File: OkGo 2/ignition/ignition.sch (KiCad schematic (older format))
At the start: 30 parts

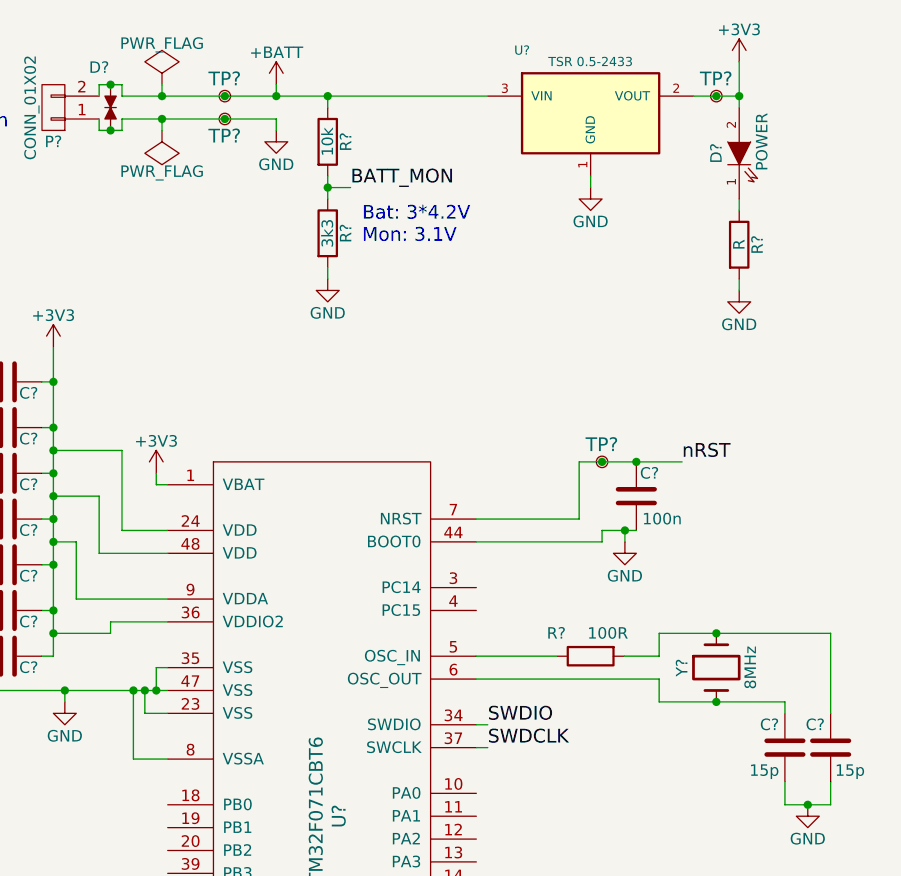
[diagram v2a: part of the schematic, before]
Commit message: Moved xtal drive resistors. Fixes #15
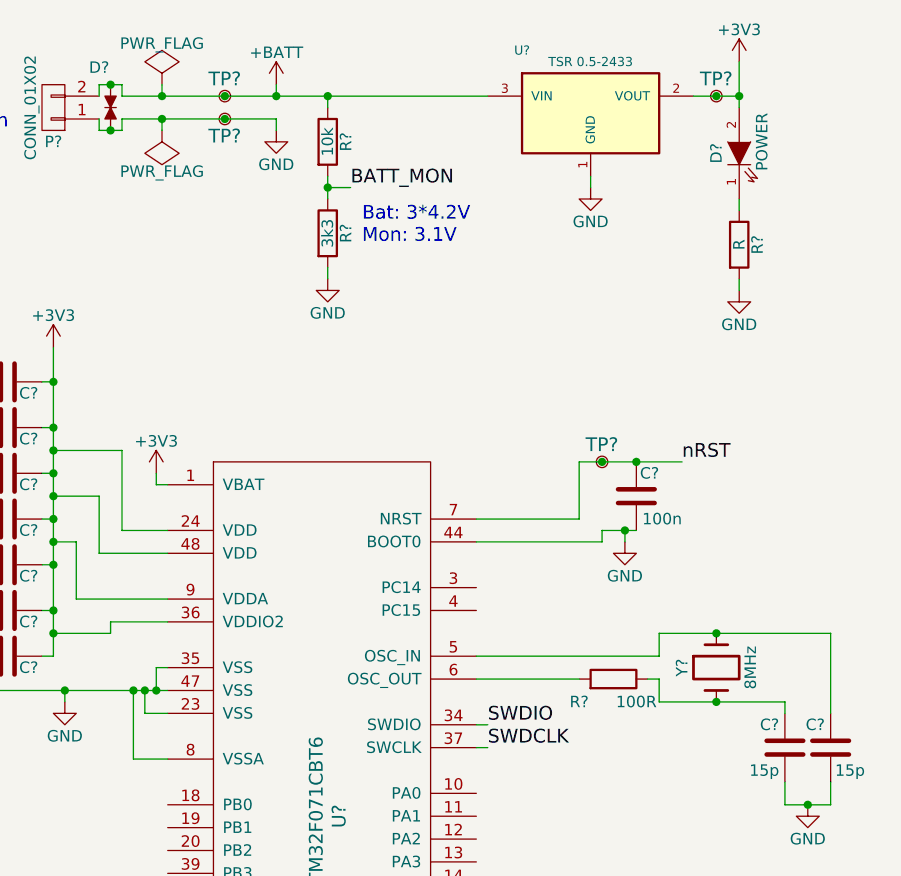
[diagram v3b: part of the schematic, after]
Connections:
- net at C?.1, Y?.1: now also U?.5 (OSC_IN); no longer R?.2
- net at C?.1, Y?.2: now also R?.1; no longer U?.6 (OSC_OUT)
- new net: R?.2, U?.6 (OSC_OUT)
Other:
- moved on the sheet: R?
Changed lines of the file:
@@
 L R R?
 U 1 1 55630D1D
-P 3450 3400
-F 0 "R?" V 3350 3550 50  0000 C CNN
-F 1 "100R" V 3350 3325 50  0000 C CNN
-F 2 "Resistors_SMD:R_0805_HandSoldering" V 3380 3400 30  0001 C CNN
-F 3 "" H 3450 3400 30  0000 C CNN
-F 4 "2331783" H 3450 3400 60  0001 C CNN "Farnell"
-	1    3450 3400
-	0    -1   1    0
+P 3550 3500
+F 0 "R?" V 3450 3350 50  0000 C CNN
+F 1 "100R" V 3450 3600 50  0000 C CNN
+F 2 "Resistors_SMD:R_0805_HandSoldering" V 3480 3500 30  0001 C CNN
+F 3 "" H 3550 3500 30  0000 C CNN
+F 4 "2331783" H 3550 3500 60  0001 C CNN "Farnell"
+	1    3550 3500
+	0    1    -1   0
 $EndComp
 $Comp
@@
 	1400 1050 1575 1050
 Wire Wire Line
-	1575 1050 2075 1050
+	1575 1050 1850 1050
+Wire Wire Line
+	1850 1050 2075 1050
 Wire Wire Line
 	2075 950  2075 900
@@
 Connection ~ 3600 2850
 Wire Wire Line
-	3400 2550 3650 2550
+	3400 2550 3500 2550
+Wire Wire Line
+	3500 2550 3650 2550
 Wire Wire Line
 	3650 2550 3850 2550
@@
 	3500 2900 2950 2900
 Wire Wire Line
-	2950 3400 3300 3400
-Wire Wire Line
-	3600 3400 3750 3400
+	2950 3400 3750 3400
 Wire Wire Line
 	3750 3400 3750 3300
@@
 Wire Wire Line
 	3750 3600 3750 3500
-Wire Wire Line
-	3750 3500 2950 3500
 Wire Wire Line
 	4300 3600 4300 3650
@@
 	1150 3550 1150 3600
 Wire Wire Line
-	3900 950  4100 950
+	3900 950  4000 950
+Wire Wire Line
+	4000 950  4100 950
 Wire Wire Line
 	1550 2600 1550 2650
@@
 	1400 950  1575 950
 Wire Wire Line
-	1575 950  2075 950
+	1575 950  1850 950
+Wire Wire Line
+	1850 950  2075 950
 Wire Wire Line
 	2075 950  2300 950
@@
 $EndComp
 Connection ~ 3500 2550
+Wire Wire Line
+	2950 3500 3400 3500
+Wire Wire Line
+	3750 3500 3700 3500
 $EndSCHEMATC

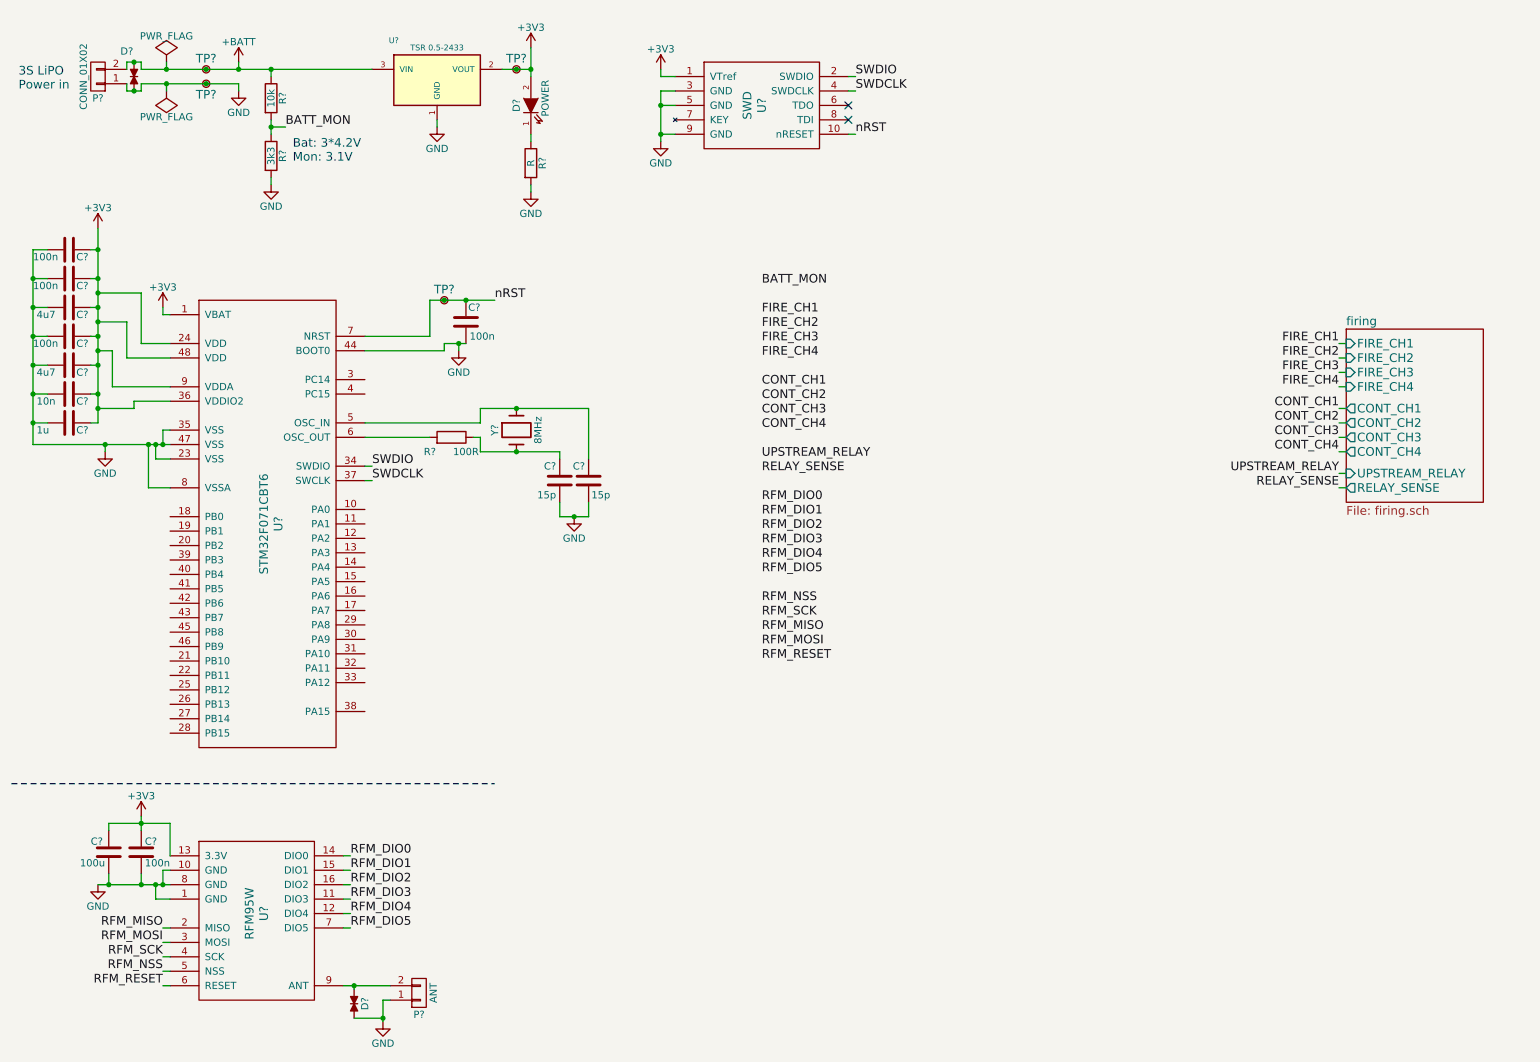
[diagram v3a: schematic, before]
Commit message: Specced/valued/footprinted a lot of parts
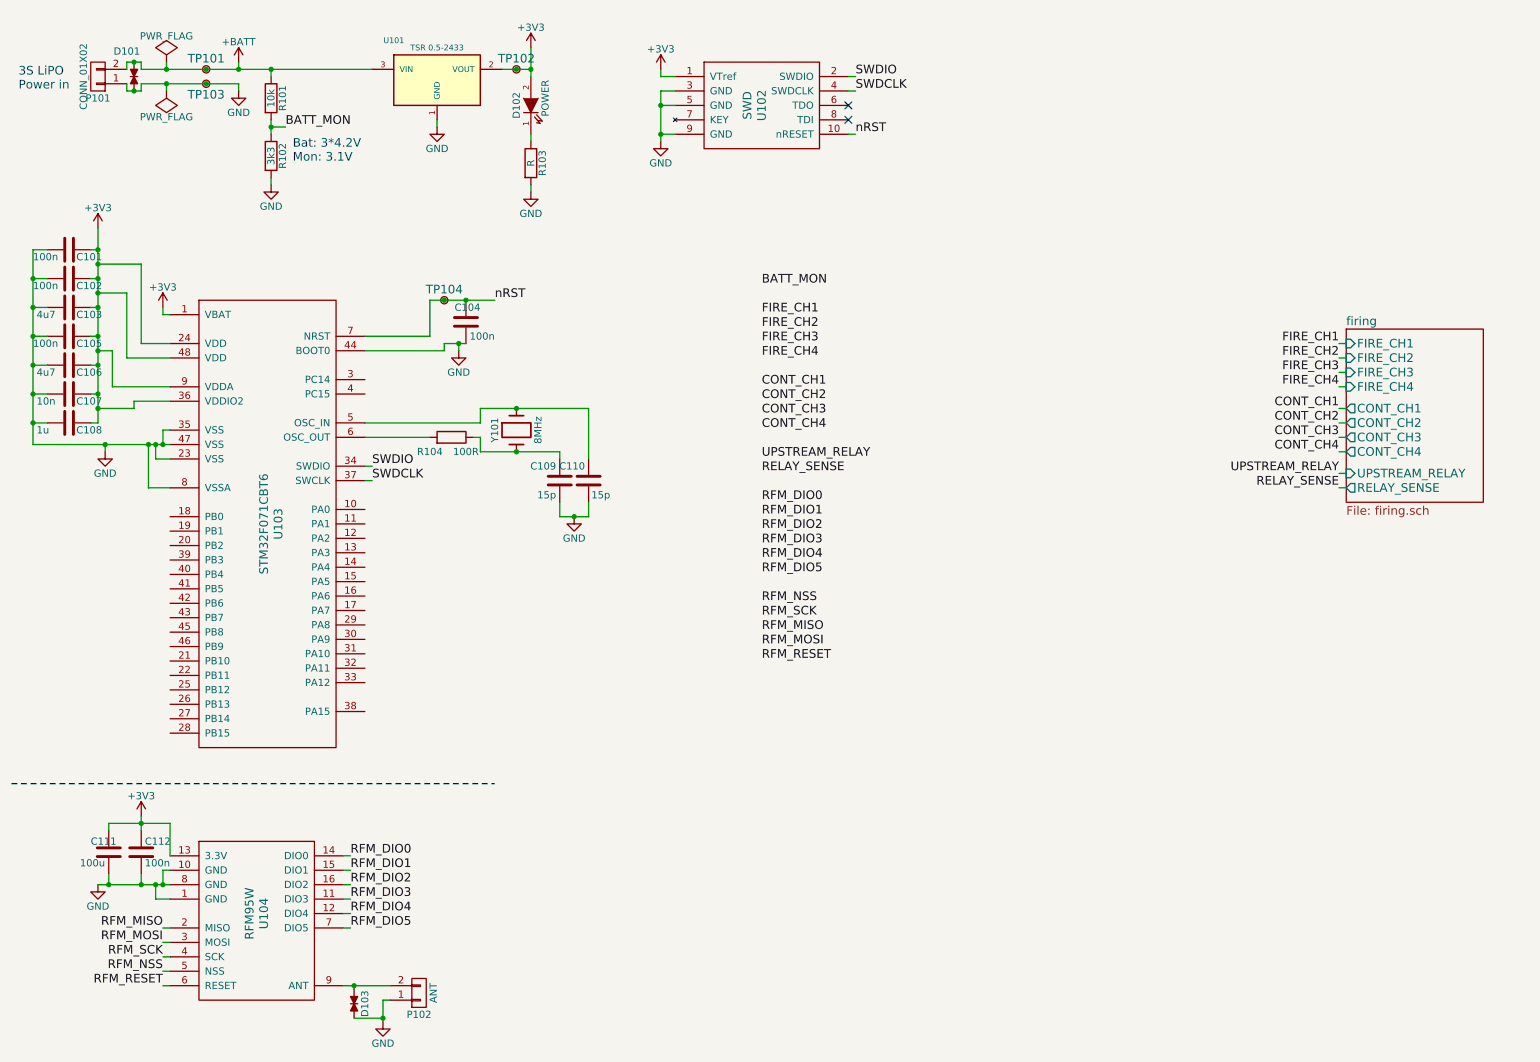
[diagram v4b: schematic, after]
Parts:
- R101: renamed from R?; Farnell 2331808 -> 9237755
- R102: renamed from R?; Farnell 2331802 -> 9237682
- U102: renamed from U?; footprint (none) -> common:FTSH-105-01-F-D-K
- U103: renamed from U?; footprint (none) -> Housings_QFP:LQFP-48_7x7mm_Pitch0.5mm; Farnell (none) -> 2432093
- gave numbers to parts that had none: 26

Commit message: Lots and lots of part selections and small mods
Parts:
- removed P102: ANT, symbol CONN_01X02
- added BT?: LiPO_3S, symbol LiPO_3S
- added F?: FUSE, symbol FUSE
- added P?: SMA, common:SMA-142-0701-801, symbol SMA
- added P? (x2): CHARGE_CASE, symbol CONN_01X04
- added P?: BATT, symbol CONN_01X02
- added P?: CHARGE_JST_XH, symbol CONN_01X04
- added SW?: Latching Push, symbol SPST_small
- P101: value CONN_01X02 -> BATT
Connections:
- net +BATT: now also F?.2; no longer D101.1, P101.2 (P2)
- net GND: now also P?.2 (GND), P?.3 (GND), P?.4 (GND), P?.5 (GND)
- net at D103.1, U104.9 (ANT): now also P?.1 (RF)
- new net: D101.1, F?.1, P101.2 (P2)
- new net: BT?.1, P?.1 (P1), P?.1 (P1)
- new net: BT?.2, P?.2 (P2)
- new net: BT?.3, P?.3 (P3)
- new net: BT?.4, P?.4 (P4), SW?.1
- new net: P?.2 (P2), SW?.2
- new net: P?.1 (P1), P?.1 (P1)
- new net: P?.2 (P2), P?.2 (P2)
- new net: P?.3 (P3), P?.3 (P3)
- new net: P?.4 (P4), P?.4 (P4)
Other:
- note removed: "3S LiPO\nPower in"
- moved on the sheet: C101, C102, C103, C104, C105, C106, C107, C108, C109, C110, C111, C112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

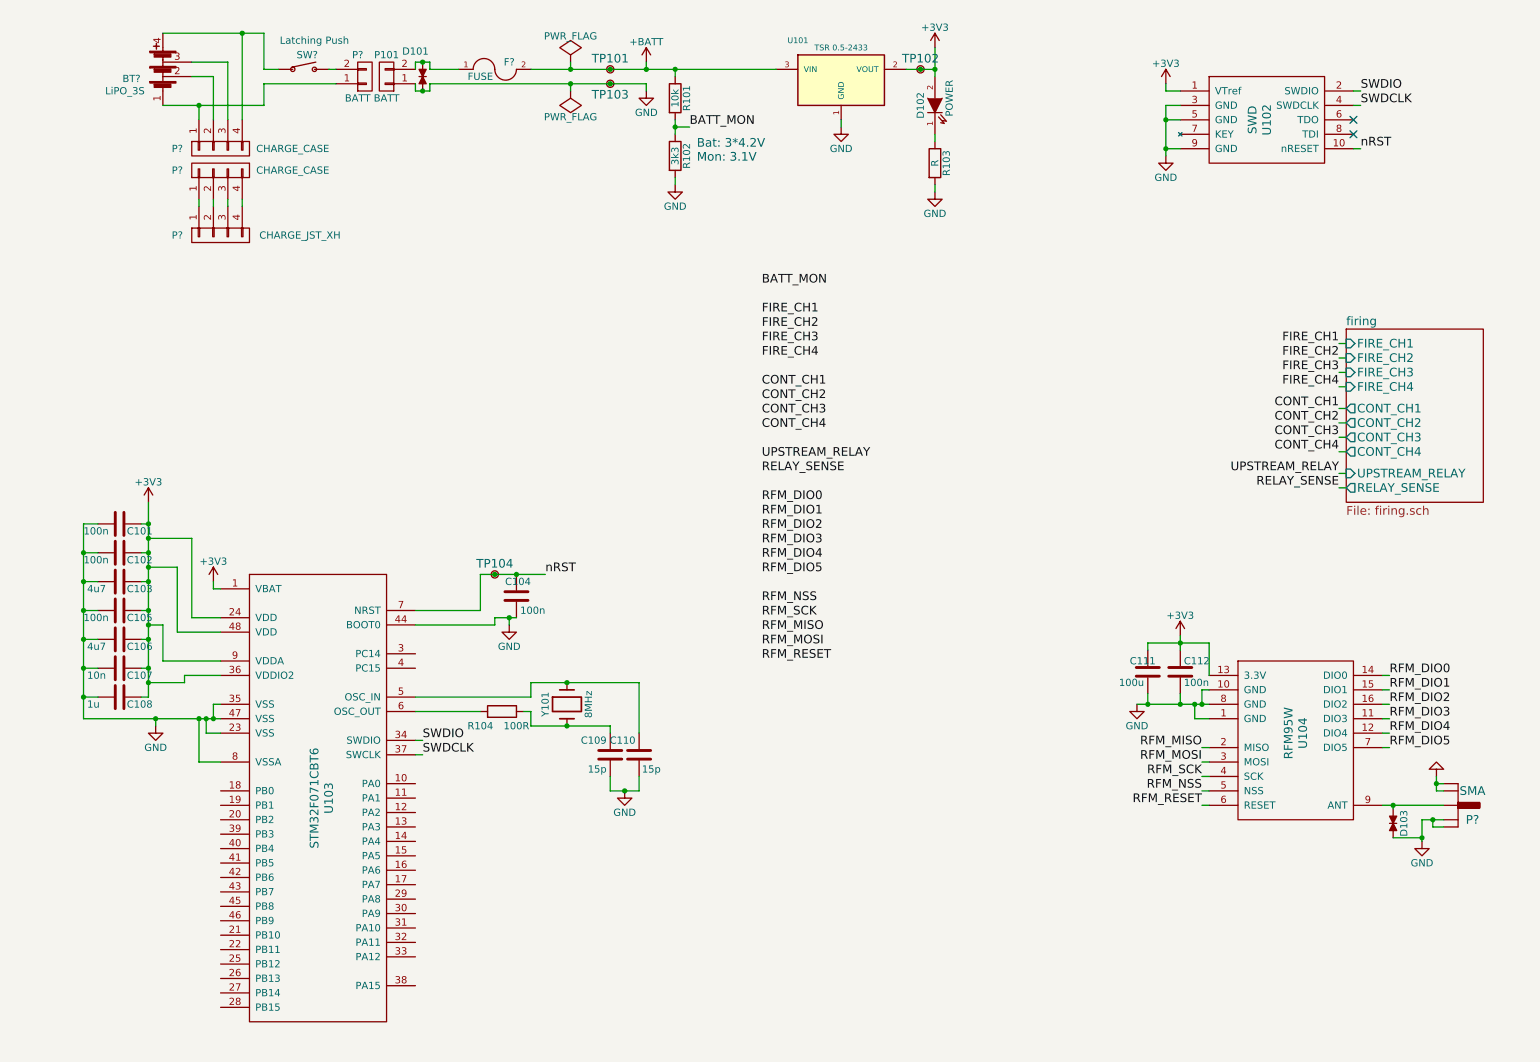
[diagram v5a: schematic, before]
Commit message: New power buttons and arm/disarm LED
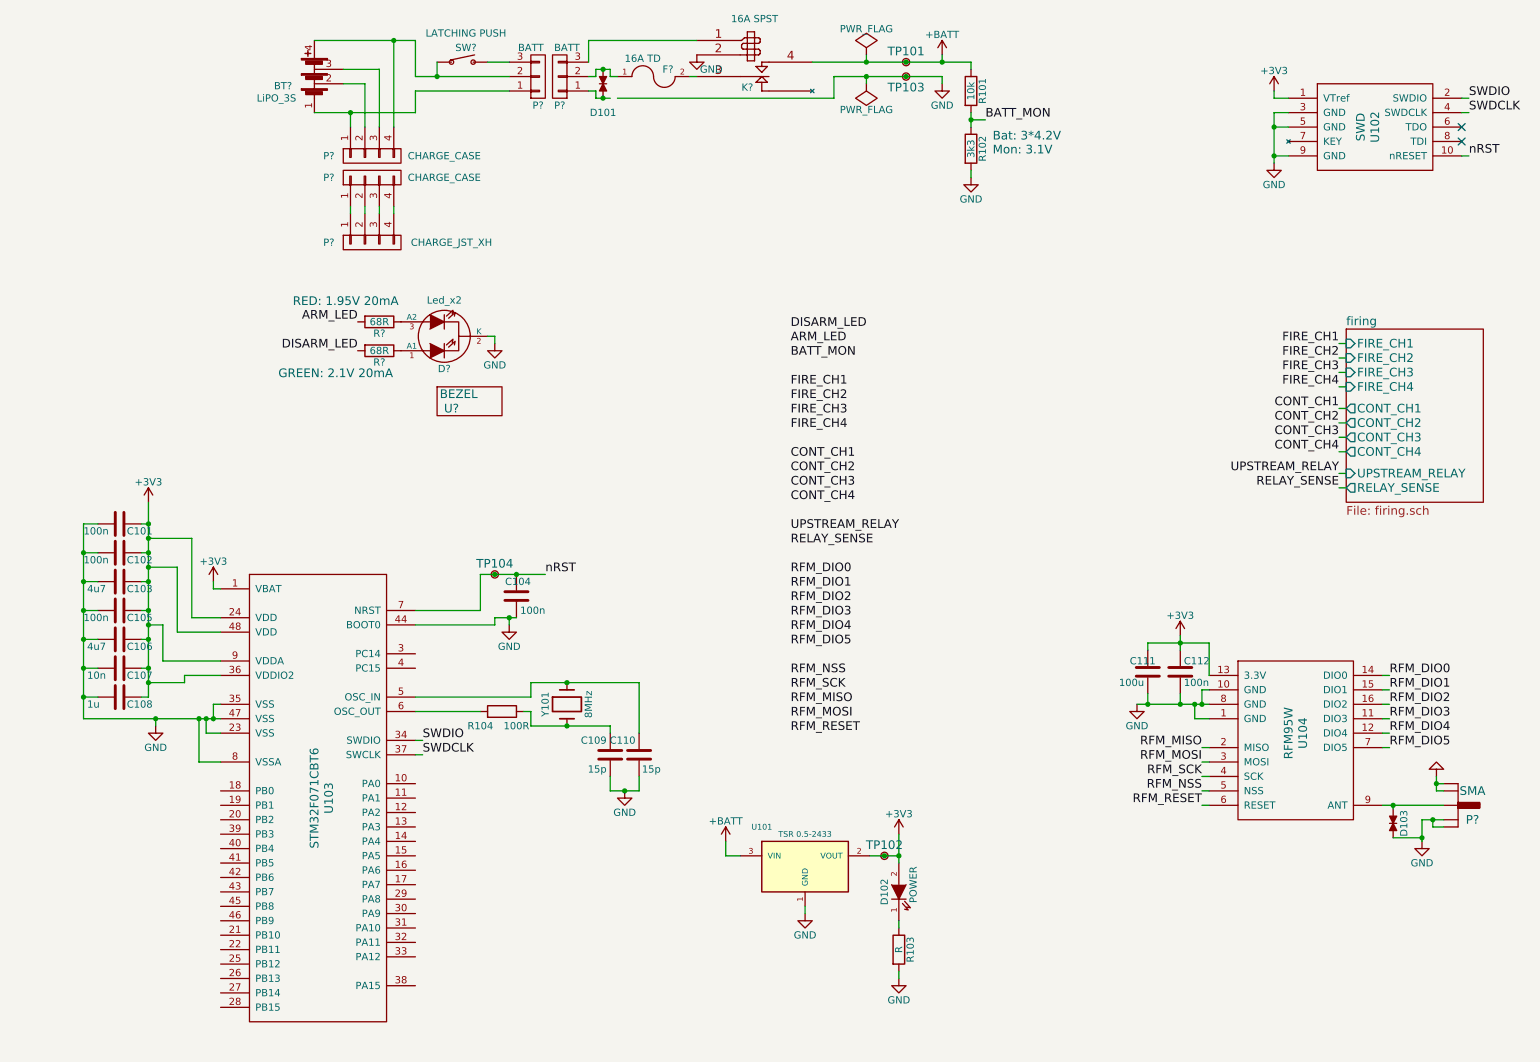
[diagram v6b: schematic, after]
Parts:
- removed P101, P?: BATT, symbol CONN_01X02
- removed SW?: Latching Push, symbol SPST_small
- added D?: Led_x2, symbol Led_x2
- added K?: 16A SPST, symbol RELAY_SPST
- added P? (x2): BATT, symbol CONN_01X03
- added R? (x2): 68R, Resistors_SMD:R_0805_HandSoldering, symbol R
- added SW?: LATCHING PUSH, symbol SPST_small
- added U?: BEZEL, symbol PART
- F?: value FUSE -> 16A TD
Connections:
- net +BATT: now also K?.4; no longer F?.2
- net GND: now also D?.2 (K), K?.2; no longer D101.2
- net at D101.1, F?.1: now also P?.2 (P2)
- net at BT?.1, P?.1 (P1): now also P?.1 (P1)
- net at BT?.4, P?.4 (P4): now also P?.2 (P2), SW?.1
- new net: D101.2, P?.1 (P1)
- new net: F?.2, K?.3
- new net: K?.1, P?.3 (P3)
- new net: P?.3 (P3), SW?.2
- new net: D?.1 (A1), R?.1
- new net: D?.3 (A2), R?.1
- new net ARM_LED: R?.2
- new net DISARM_LED: R?.2
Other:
- note added: "GREEN: 2.1V 20mA"
- note added: "RED: 1.95V 20mA"
- moved on the sheet: BT?, D101, D102, F?, P?, R101, R102, R103, TP101, TP102, TP103, U101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

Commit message: Lots of footprinting.
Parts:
- added U?: FUSE 15A, symbol PART
- added U?: CLIP, symbol PART
- BT101: renamed from BT?; URL (none) -> http://hobbyking.com/hobbyking/store/uh_viewItem.asp?idProd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
- F101: renamed from F?; value 16A TD -> 6.3x32; footprint (none) -> ignition:6x32_fuseclip; Farnell (none) -> 1603990
- Y101: footprint (none) -> common:XTAL50x32
- gave numbers to parts that had none: 12
- renumbered C111 to C108, C112 to C109, C108 to C110, C109 to C111, C110 to C112, D102 to D104, R104 to R105, R103 to R106, TP103 to TP102, TP104 to TP103, TP102 to TP104, U102 to U101, U104 to U103, U103 to U104, U101 to U105
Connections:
- net GND: now also D101.2, P102.1 (P1)
